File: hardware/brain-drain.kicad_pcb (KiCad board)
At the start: 4 copper layers, 180 x 110 mm, 310 parts, among them J10 SATA 22-pin, J11 SATA 22-pin, J12 SATA 22-pin, J13 SATA 22-pin, J21 KPJX-4S-S, J3 microSD, J4 RJ45 GbE magjack UDE RB1-125B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, J40 Fan GND/5V/TACH/PWM, J41 OLED GND/VCC/SCL/SDA, J5 USB-C rpiboot, J50 M.2 M-key, J6 nRPIBOOT, J7 UART0 GND/TX/RX, M1 CM5002016 (J1), M2 CM5002016 (J2), Q1 2N7002, Q20 AO4407A, Q31 P-FET -30V 6A DFN3x3, Q32 P-FET -30V 6A DFN3x3, Q33 P-FET -30V 6A DFN3x3, Q34 P-FET -30V 6A DFN3x3, Q41 P-FET -30V 6A DFN3x3, Q42 P-FET -30V 6A DFN3x3, Q43 P-FET -30V 6A DFN3x3, Q44 P-FET -30V 6A DFN3x3, Q51 2N7002, Q52 2N7002, Q53 2N7002, Q54 2N7002, Q61 2N7002, Q62 2N7002, Q63 2N7002, Q64 2N7002, SW1 DIP x8, SW3 door microswitch, U1 USB5744/2G, U10 ASM1153E, U11 ASM1153E, U12 ASM1153E, U13 ASM1153E, U2 USB5744/2G, U20 TPS56637RPAR, U21 TPS56637RPAR, U22 AP63203WU-7, U3 AP2112K-1.2, U50 TPS22965DSGR, U51 AP63203WU-7, Y1 25MHz CL=20pF, Y10 30MHz CL=16pF, Y11 30MHz CL=16pF, Y12 30MHz CL=16pF, Y13 30MHz CL=16pF, Y2 25MHz CL=20pF

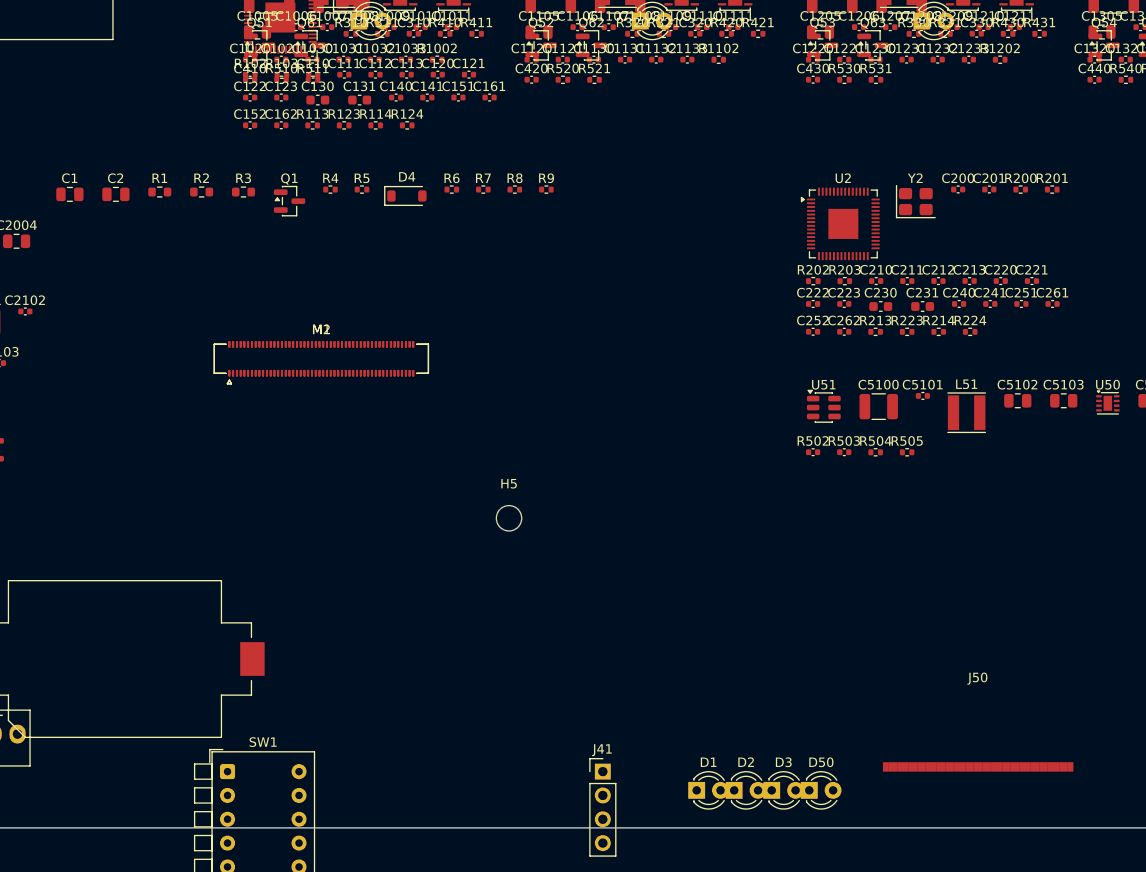
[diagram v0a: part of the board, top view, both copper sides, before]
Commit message: hardware: CM5 on the official 204-pad footprint, CM5IO M.2 footprint, reference-design fixes
From the Raspberry Pi CM5IO rev 2 KiCad files: single CM5 footprint with both
connectors and mounting holes; M.2 socket footprint; USB-C CC pins to the CM5;
fan PWM pull-up; microSD through a load switch on SD_PWR_ON; M.2 shield and
standoff pads to GND; PCIe polarity note. Board regenerated with the module
and M.2 at their real sizes; centre mounting hole dropped.

Co-Authored-By: Claude Fable 5.1 <noreply@anthropic.com>
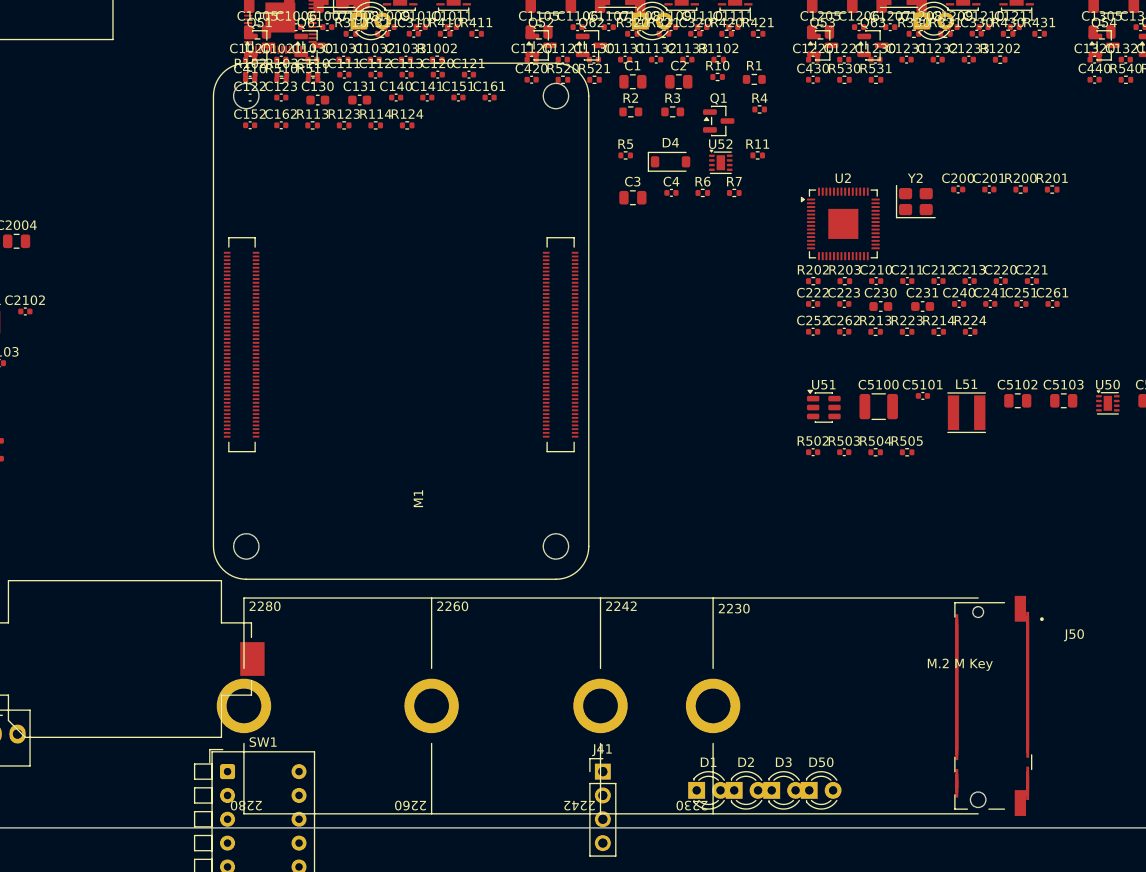
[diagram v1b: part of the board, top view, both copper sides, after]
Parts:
- added SW3: door microswitch, Button_Switch_THT:SW_PUSH_6mm, F.Cu at (196.0, 110.0)
- BT1: renamed from C1; value 22u 10V -> CR2032; footprint Capacitor_SMD:C_0805_2012Metric -> Battery:BatteryHolder_Keystone_1060_1x2032
- BZ1: renamed from SW1; value DIP x8 -> 5V magnetic; footprint Button_Switch_THT:SW_DIP_SPSTx08_Piano_10.8x21.88mm_W7.62mm_P2.54mm -> Buzzer_Beeper:Buzzer_12x9.5RM7.6
- C1: renamed from M1; value CM5002016 (J1) -> 22u 10V; footprint Connector_Hirose_DF40:Hirose_DF40C-100DS-0.4V_2x50_P0.4mm -> Capacitor_SMD:C_0805_2012Metric
- C1001: renamed from R1000; value 12.1k 1% -> 22p; footprint Resistor_SMD:R_0402_1005Metric -> Capacitor_SMD:C_0402_1005Metric
- C1002: renamed from L10; value 4.7u 1A -> 2.2u; footprint Inductor_SMD:L_Taiyo-Yuden_NR-40xx -> Capacitor_SMD:C_0603_1608Metric
- C1005: renamed from C1006; value 100n -> 10u 10V; footprint Capacitor_SMD:C_0402_1005Metric -> Capacitor_SMD:C_0805_2012Metric
- C101: renamed from R100; value 12.0k 1% -> 33p; footprint Resistor_SMD:R_0402_1005Metric -> Capacitor_SMD:C_0402_1005Metric
- C1021: renamed from C1030; value 10n -> 100n
- C1033: renamed from D10; value blue bay activity -> 10n; footprint LED_THT:LED_D3.0mm -> Capacitor_SMD:C_0402_1005Metric
- C1101: renamed from R1100; value 12.1k 1% -> 22p; footprint Resistor_SMD:R_0402_1005Metric -> Capacitor_SMD:C_0402_1005Metric
- C1102: renamed from L11; value 4.7u 1A -> 2.2u; footprint Inductor_SMD:L_Taiyo-Yuden_NR-40xx -> Capacitor_SMD:C_0603_1608Metric
- C1105: renamed from C1106; value 100n -> 10u 10V; footprint Capacitor_SMD:C_0402_1005Metric -> Capacitor_SMD:C_0805_2012Metric
- C1121: renamed from C1130; value 10n -> 100n
- C1133: renamed from D11; value blue bay activity -> 10n; footprint LED_THT:LED_D3.0mm -> Capacitor_SMD:C_0402_1005Metric
- C1201: renamed from R1200; value 12.1k 1% -> 22p; footprint Resistor_SMD:R_0402_1005Metric -> Capacitor_SMD:C_0402_1005Metric
- C1202: renamed from L12; value 4.7u 1A -> 2.2u; footprint Inductor_SMD:L_Taiyo-Yuden_NR-40xx -> Capacitor_SMD:C_0603_1608Metric
- C1205: renamed from C1206; value 100n -> 10u 10V; footprint Capacitor_SMD:C_0402_1005Metric -> Capacitor_SMD:C_0805_2012Metric
- C1221: renamed from C1230; value 10n -> 100n
- C123: renamed from C130; value 4.7u 10V -> 100n; footprint Capacitor_SMD:C_0603_1608Metric -> Capacitor_SMD:C_0402_1005Metric
- C1233: renamed from D12; value blue bay activity -> 10n; footprint LED_THT:LED_D3.0mm -> Capacitor_SMD:C_0402_1005Metric
- C1301: renamed from R1300; value 12.1k 1% -> 22p; footprint Resistor_SMD:R_0402_1005Metric -> Capacitor_SMD:C_0402_1005Metric
- C1302: renamed from L13; value 4.7u 1A -> 2.2u; footprint Inductor_SMD:L_Taiyo-Yuden_NR-40xx -> Capacitor_SMD:C_0603_1608Metric
- C1305: renamed from C1306; value 100n -> 10u 10V; footprint Capacitor_SMD:C_0402_1005Metric -> Capacitor_SMD:C_0805_2012Metric
- C131: renamed from C140; value 100n -> 4.7u 10V; footprint Capacitor_SMD:C_0402_1005Metric -> Capacitor_SMD:C_0603_1608Metric
- C1321: renamed from C1330; value 10n -> 100n
- C1333: renamed from D13; value blue bay activity -> 10n; footprint LED_THT:LED_D3.0mm -> Capacitor_SMD:C_0402_1005Metric
- C162: renamed from R113; value 10k -> 100n; footprint Resistor_SMD:R_0402_1005Metric -> Capacitor_SMD:C_0402_1005Metric
- C2: renamed from M2; value CM5002016 (J2) -> 22u 10V; footprint Connector_Hirose_DF40:Hirose_DF40C-100DS-0.4V_2x50_P0.4mm -> Capacitor_SMD:C_0805_2012Metric
- C20: renamed from D21; value 12V 0.5W -> 680u 25V low-ESR; footprint Diode_SMD:D_SOD-123 -> Capacitor_SMD:CP_Elec_10x10.5
- C2000: renamed from U20; value TPS56637RPAR -> 10u 25V; footprint brain-drain:Texas_RPA0010A_VQFN-HR-10_3x3mm -> Capacitor_SMD:C_1210_3225Metric
- C2002: renamed from C2001; value 10u 25V -> 100n 25V; footprint Capacitor_SMD:C_1210_3225Metric -> Capacitor_SMD:C_0402_1005Metric
- C2003: renamed from L20; value 2.2u 8A -> 22u 10V; footprint Inductor_SMD:L_Taiyo-Yuden_NR-60xx -> Capacitor_SMD:C_0805_2012Metric
- C201: renamed from R200; value 12.0k 1% -> 33p; footprint Resistor_SMD:R_0402_1005Metric -> Capacitor_SMD:C_0402_1005Metric
- C2100: renamed from U21; value TPS56637RPAR -> 10u 25V; footprint brain-drain:Texas_RPA0010A_VQFN-HR-10_3x3mm -> Capacitor_SMD:C_1210_3225Metric
- C2102: renamed from C2101; value 10u 25V -> 100n 25V; footprint Capacitor_SMD:C_1210_3225Metric -> Capacitor_SMD:C_0402_1005Metric
- C2103: renamed from L21; value 2.2u 8A -> 22u 10V; footprint Inductor_SMD:L_Taiyo-Yuden_NR-60xx -> Capacitor_SMD:C_0805_2012Metric
- C22: renamed from C21; value 680u 25V low-ESR -> 10u 25V; footprint Capacitor_SMD:CP_Elec_10x10.5 -> Capacitor_SMD:C_1210_3225Metric
- C2200: renamed from U22; value AP63203WU-7 -> 10u 25V; footprint Package_TO_SOT_SMD:TSOT-23-6 -> Capacitor_SMD:C_1210_3225Metric
- C2201: renamed from C2200; value 10u 25V -> 100n 10V; footprint Capacitor_SMD:C_1210_3225Metric -> Capacitor_SMD:C_0402_1005Metric
- C2202: renamed from L22; value 4.7u 3A -> 22u 10V; footprint Inductor_SMD:L_Taiyo-Yuden_NR-40xx -> Capacitor_SMD:C_0805_2012Metric
- C223: renamed from C230; value 4.7u 10V -> 100n; footprint Capacitor_SMD:C_0603_1608Metric -> Capacitor_SMD:C_0402_1005Metric
- C231: renamed from C240; value 100n -> 4.7u 10V; footprint Capacitor_SMD:C_0402_1005Metric -> Capacitor_SMD:C_0603_1608Metric
- C262: renamed from R213; value 10k -> 100n; footprint Resistor_SMD:R_0402_1005Metric -> Capacitor_SMD:C_0402_1005Metric
- C3: renamed from R6; value 470 -> 10u 10V; footprint Resistor_SMD:R_0402_1005Metric -> Capacitor_SMD:C_0805_2012Metric
- C30: renamed from U3; value AP2112K-1.2 -> 1u 10V; footprint Package_TO_SOT_SMD:SOT-23-5 -> Capacitor_SMD:C_0402_1005Metric
- C31: renamed from C30; value 1u 10V -> 10u 10V; footprint Capacitor_SMD:C_0402_1005Metric -> Capacitor_SMD:C_0805_2012Metric
- C310: renamed from R410; value 100k -> 100n; footprint Resistor_SMD:R_0402_1005Metric -> Capacitor_SMD:C_0402_1005Metric
- C320: renamed from R420; value 100k -> 100n; footprint Resistor_SMD:R_0402_1005Metric -> Capacitor_SMD:C_0402_1005Metric
- C330: renamed from R430; value 100k -> 100n; footprint Resistor_SMD:R_0402_1005Metric -> Capacitor_SMD:C_0402_1005Metric
- C340: renamed from R440; value 100k -> 100n; footprint Resistor_SMD:R_0402_1005Metric -> Capacitor_SMD:C_0402_1005Metric
- C4: renamed from R7; value 470 -> 1u 10V; footprint Resistor_SMD:R_0402_1005Metric -> Capacitor_SMD:C_0402_1005Metric
- C410: renamed from R510; value 10k -> 100n; footprint Resistor_SMD:R_0402_1005Metric -> Capacitor_SMD:C_0402_1005Metric
- C420: renamed from R520; value 10k -> 100n; footprint Resistor_SMD:R_0402_1005Metric -> Capacitor_SMD:C_0402_1005Metric
- C430: renamed from R530; value 10k -> 100n; footprint Resistor_SMD:R_0402_1005Metric -> Capacitor_SMD:C_0402_1005Metric
- C440: renamed from R540; value 10k -> 100n; footprint Resistor_SMD:R_0402_1005Metric -> Capacitor_SMD:C_0402_1005Metric
- C500: renamed from C501; value 22u 10V -> 10u 10V
- C501: renamed from C502; value 1n -> 22u 10V; footprint Capacitor_SMD:C_0402_1005Metric -> Capacitor_SMD:C_0805_2012Metric
- C502: renamed from R500; value 10k -> 1n; footprint Resistor_SMD:R_0402_1005Metric -> Capacitor_SMD:C_0402_1005Metric
- C5100: renamed from U51; value AP63203WU-7 -> 10u 25V; footprint Package_TO_SOT_SMD:TSOT-23-6 -> Capacitor_SMD:C_1210_3225Metric
- C5101: renamed from C5100; value 10u 25V -> 100n 10V; footprint Capacitor_SMD:C_1210_3225Metric -> Capacitor_SMD:C_0402_1005Metric
- C5102: renamed from L51; value 4.7u 3A -> 22u 10V; footprint Inductor_SMD:L_Taiyo-Yuden_NR-40xx -> Capacitor_SMD:C_0805_2012Metric
- D1: renamed from J40; value Fan GND/5V/TACH/PWM -> green PWR; footprint Connector:FanPinHeader_1x04_P2.54mm_Vertical -> LED_THT:LED_D3.0mm
- D10: renamed from R1002; value 470 -> blue bay activity; footprint Resistor_SMD:R_0402_1005Metric -> LED_THT:LED_D3.0mm
- D11: renamed from R1102; value 470 -> blue bay activity; footprint Resistor_SMD:R_0402_1005Metric -> LED_THT:LED_D3.0mm
- D12: renamed from R1202; value 470 -> blue bay activity; footprint Resistor_SMD:R_0402_1005Metric -> LED_THT:LED_D3.0mm
- D13: renamed from R1302; value 470 -> blue bay activity; footprint Resistor_SMD:R_0402_1005Metric -> LED_THT:LED_D3.0mm
- D2: renamed from R1; value 1k -> green ACT; footprint Resistor_SMD:R_0603_1608Metric -> LED_THT:LED_D3.0mm
- D20: renamed from F1; value 10A slow 0453010.MR -> SMBJ15A; footprint Fuse:Fuse_Littelfuse-NANO2-451_453 -> Diode_SMD:D_SMB
- D21: renamed from R20; value 100k -> 12V 0.5W; footprint Resistor_SMD:R_0603_1608Metric -> Diode_SMD:D_SOD-123
- D3: renamed from R2; value 1k -> red STATUS; footprint Resistor_SMD:R_0603_1608Metric -> LED_THT:LED_D3.0mm
- D4: renamed from R5; value 100k -> 1N4148W; footprint Resistor_SMD:R_0402_1005Metric -> Diode_SMD:D_SOD-123
- D50: renamed from SW3; value door microswitch -> blue M.2 activity; footprint Button_Switch_THT:SW_PUSH_6mm -> LED_THT:LED_D3.0mm
- F1: renamed from J21; value KPJX-4S-S -> 10A slow 0453010.MR; footprint brain-drain:Kycon_KPJX-4S-S -> Fuse:Fuse_Littelfuse-NANO2-451_453
- F10: renamed from F14; value 2A hold 1812 -> 3A hold 1812
- F11: renamed from F15; value 2A hold 1812 -> 3A hold 1812
- F12: renamed from F16; value 2A hold 1812 -> 3A hold 1812
- F13: renamed from F17; value 2A hold 1812 -> 3A hold 1812
- F14: renamed from U11; value ASM1153E -> 2A hold 1812; footprint Package_DFN_QFN:QFN-48-1EP_6x6mm_P0.4mm_EP4.6x4.6mm -> Fuse:Fuse_1812_4532Metric
- F15: renamed from U12; value ASM1153E -> 2A hold 1812; footprint Package_DFN_QFN:QFN-48-1EP_6x6mm_P0.4mm_EP4.6x4.6mm -> Fuse:Fuse_1812_4532Metric
- F16: renamed from U13; value ASM1153E -> 2A hold 1812; footprint Package_DFN_QFN:QFN-48-1EP_6x6mm_P0.4mm_EP4.6x4.6mm -> Fuse:Fuse_1812_4532Metric
- F17: renamed from Q31; value P-FET -30V 6A DFN3x3 -> 2A hold 1812; footprint Package_DFN_QFN:DFN-8-1EP_3x3mm_P0.65mm_EP1.5x2.25mm -> Fuse:Fuse_1812_4532Metric
- J10: renamed from Y10; value 30MHz CL=16pF -> SATA 22-pin; footprint Crystal:Crystal_SMD_3225-4Pin_3.2x2.5mm -> brain-drain:SATA_22pin_Receptacle_RA
- J11: renamed from Y11; value 30MHz CL=16pF -> SATA 22-pin; footprint Crystal:Crystal_SMD_3225-4Pin_3.2x2.5mm -> brain-drain:SATA_22pin_Receptacle_RA
- J12: renamed from Y12; value 30MHz CL=16pF -> SATA 22-pin; footprint Crystal:Crystal_SMD_3225-4Pin_3.2x2.5mm -> brain-drain:SATA_22pin_Receptacle_RA
- J13: renamed from Y13; value 30MHz CL=16pF -> SATA 22-pin; footprint Crystal:Crystal_SMD_3225-4Pin_3.2x2.5mm -> brain-drain:SATA_22pin_Receptacle_RA
- J21: renamed from H5; value M2.5 -> KPJX-4S-S; footprint MountingHole:MountingHole_2.7mm_M2.5 -> brain-drain:Kycon_KPJX-4S-S
- J3: renamed from J41; value OLED GND/VCC/SCL/SDA -> microSD; footprint Connector_PinHeader_2.54mm:PinHeader_1x04_P2.54mm_Vertical -> Connector_Card:microSD_HC_Hirose_DM3AT-SF-PEJM5
- J4: renamed from J5; value USB-C rpiboot -> RJ45 GbE magjack UDE RB1-125B8G1A; footprint Connector_USB:USB_C_Receptacle_GCT_USB4085 -> Connector_RJ:RJ45_UDE_RB1-125B8G1A
- J40: renamed from J6; value nRPIBOOT -> Fan GND/5V/TACH/PWM; footprint Connector_PinHeader_2.54mm:PinHeader_1x02_P2.54mm_Vertical -> Connector:FanPinHeader_1x04_P2.54mm_Vertical
- J41: renamed from D4; value 1N4148W -> OLED GND/VCC/SCL/SDA; footprint Diode_SMD:D_SOD-123 -> Connector_PinHeader_2.54mm:PinHeader_1x04_P2.54mm_Vertical
- J5: renamed from U1; value USB5744/2G -> USB-C rpiboot; footprint Package_DFN_QFN:QFN-56-1EP_7x7mm_P0.4mm_EP3.2x3.2mm -> Connector_USB:USB_C_Receptacle_GCT_USB4085
- J50: renamed from U50; value TPS22965DSGR -> M.2 M-key; footprint Package_SON:Texas_DSG0008A_WSON-8-1EP_2x2mm_P0.5mm_EP0.9x1.6mm -> brain-drain:M2_Socket3_MKey_CM5IO
- J6: renamed from C2; value 22u 10V -> nRPIBOOT; footprint Capacitor_SMD:C_0805_2012Metric -> Connector_PinHeader_2.54mm:PinHeader_1x02_P2.54mm_Vertical
- J7: renamed from BT1; value CR2032 -> UART0 GND/TX/RX; footprint Battery:BatteryHolder_Keystone_1060_1x2032 -> Connector_PinHeader_2.54mm:PinHeader_1x03_P2.54mm_Vertical
- L10: renamed from C1003; value 10u 10V -> 4.7u 1A; footprint Capacitor_SMD:C_0805_2012Metric -> Inductor_SMD:L_Taiyo-Yuden_NR-40xx
- L11: renamed from C1103; value 10u 10V -> 4.7u 1A; footprint Capacitor_SMD:C_0805_2012Metric -> Inductor_SMD:L_Taiyo-Yuden_NR-40xx
- L12: renamed from C1203; value 10u 10V -> 4.7u 1A; footprint Capacitor_SMD:C_0805_2012Metric -> Inductor_SMD:L_Taiyo-Yuden_NR-40xx
- L13: renamed from C1303; value 10u 10V -> 4.7u 1A; footprint Capacitor_SMD:C_0805_2012Metric -> Inductor_SMD:L_Taiyo-Yuden_NR-40xx
- L20: renamed from C2002; value 100n 25V -> 2.2u 8A; footprint Capacitor_SMD:C_0402_1005Metric -> Inductor_SMD:L_Taiyo-Yuden_NR-60xx
- L21: renamed from C2102; value 100n 25V -> 2.2u 8A; footprint Capacitor_SMD:C_0402_1005Metric -> Inductor_SMD:L_Taiyo-Yuden_NR-60xx
- L22: renamed from C2201; value 100n 10V -> 4.7u 3A; footprint Capacitor_SMD:C_0402_1005Metric -> Inductor_SMD:L_Taiyo-Yuden_NR-40xx
- L51: renamed from C5101; value 100n 10V -> 4.7u 3A; footprint Capacitor_SMD:C_0402_1005Metric -> Inductor_SMD:L_Taiyo-Yuden_NR-40xx
- M1: renamed from C31; value 10u 10V -> CM5002016; footprint Capacitor_SMD:C_0805_2012Metric -> brain-drain:Raspberry-Pi-5-Compute-Module
- Q1: renamed from BZ1; value 5V magnetic -> 2N7002; footprint Buzzer_Beeper:Buzzer_12x9.5RM7.6 -> Package_TO_SOT_SMD:SOT-23
- Q20: renamed from D20; value SMBJ15A -> AO4407A; footprint Diode_SMD:D_SMB -> Package_SO:SOIC-8_3.9x4.9mm_P1.27mm
- Q41: renamed from Q51; value 2N7002 -> P-FET -30V 6A DFN3x3; footprint Package_TO_SOT_SMD:SOT-23 -> Package_DFN_QFN:DFN-8-1EP_3x3mm_P0.65mm_EP1.5x2.25mm
- Q42: renamed from Q52; value 2N7002 -> P-FET -30V 6A DFN3x3; footprint Package_TO_SOT_SMD:SOT-23 -> Package_DFN_QFN:DFN-8-1EP_3x3mm_P0.65mm_EP1.5x2.25mm
- Q43: renamed from Q53; value 2N7002 -> P-FET -30V 6A DFN3x3; footprint Package_TO_SOT_SMD:SOT-23 -> Package_DFN_QFN:DFN-8-1EP_3x3mm_P0.65mm_EP1.5x2.25mm
- Q44: renamed from Q54; value 2N7002 -> P-FET -30V 6A DFN3x3; footprint Package_TO_SOT_SMD:SOT-23 -> Package_DFN_QFN:DFN-8-1EP_3x3mm_P0.65mm_EP1.5x2.25mm
- Q61: renamed from R310; value 100k -> 2N7002; footprint Resistor_SMD:R_0402_1005Metric -> Package_TO_SOT_SMD:SOT-23
- Q62: renamed from R320; value 100k -> 2N7002; footprint Resistor_SMD:R_0402_1005Metric -> Package_TO_SOT_SMD:SOT-23
- Q63: renamed from R330; value 100k -> 2N7002; footprint Resistor_SMD:R_0402_1005Metric -> Package_TO_SOT_SMD:SOT-23
- Q64: renamed from R340; value 100k -> 2N7002; footprint Resistor_SMD:R_0402_1005Metric -> Package_TO_SOT_SMD:SOT-23
- R1: renamed from D1; value green PWR -> 1k; footprint LED_THT:LED_D3.0mm -> Resistor_SMD:R_0603_1608Metric
- R10: renamed from J7; value UART0 GND/TX/RX -> 10k; footprint Connector_PinHeader_2.54mm:PinHeader_1x03_P2.54mm_Vertical -> Resistor_SMD:R_0402_1005Metric
- R100: renamed from R101; value 10k -> 12.0k 1%
- R1000: renamed from R1001; value 10k -> 12.1k 1%
- R1001: renamed from C1002; value 2.2u -> 10k; footprint Capacitor_SMD:C_0603_1608Metric -> Resistor_SMD:R_0402_1005Metric
- R1002: renamed from F10; value 3A hold 1812 -> 470; footprint Fuse:Fuse_1812_4532Metric -> Resistor_SMD:R_0402_1005Metric
- R102: renamed from R103; value 200k -> 10k
- R103: renamed from C110; value 100n -> 200k; footprint Capacitor_SMD:C_0402_1005Metric -> Resistor_SMD:R_0402_1005Metric
- R11: renamed from J4; value RJ45 GbE magjack UDE RB1-125B8G1A -> 10k; footprint Connector_RJ:RJ45_UDE_RB1-125B8G1A -> Resistor_SMD:R_0402_1005Metric
- R1100: renamed from R1101; value 10k -> 12.1k 1%
- R1101: renamed from C1102; value 2.2u -> 10k; footprint Capacitor_SMD:C_0603_1608Metric -> Resistor_SMD:R_0402_1005Metric
- R1102: renamed from F11; value 3A hold 1812 -> 470; footprint Fuse:Fuse_1812_4532Metric -> Resistor_SMD:R_0402_1005Metric
- R1200: renamed from R1201; value 10k -> 12.1k 1%
- R1201: renamed from C1202; value 2.2u -> 10k; footprint Capacitor_SMD:C_0603_1608Metric -> Resistor_SMD:R_0402_1005Metric
- R1202: renamed from F12; value 3A hold 1812 -> 470; footprint Fuse:Fuse_1812_4532Metric -> Resistor_SMD:R_0402_1005Metric
- R124: renamed from U2; value USB5744/2G -> 10k; footprint Package_DFN_QFN:QFN-56-1EP_7x7mm_P0.4mm_EP3.2x3.2mm -> Resistor_SMD:R_0402_1005Metric
- R1300: renamed from R1301; value 10k -> 12.1k 1%
- R1301: renamed from C1302; value 2.2u -> 10k; footprint Capacitor_SMD:C_0603_1608Metric -> Resistor_SMD:R_0402_1005Metric
- R1302: renamed from F13; value 3A hold 1812 -> 470; footprint Fuse:Fuse_1812_4532Metric -> Resistor_SMD:R_0402_1005Metric
- R2: renamed from D2; value green ACT -> 1k; footprint LED_THT:LED_D3.0mm -> Resistor_SMD:R_0603_1608Metric
- R20: renamed from Q20; value AO4407A -> 100k; footprint Package_SO:SOIC-8_3.9x4.9mm_P1.27mm -> Resistor_SMD:R_0603_1608Metric
- R200: renamed from R201; value 10k -> 12.0k 1%
- R2000: renamed from C2005; value 22u 10V -> 73.2k; footprint Capacitor_SMD:C_0805_2012Metric -> Resistor_SMD:R_0402_1005Metric
- R2001: renamed from R2000; value 73.2k -> 10k
- R2002: renamed from R2001; value 10k -> 100k
- R2003: renamed from R2002; value 100k -> 10k
- R202: renamed from R203; value 200k -> 10k
- R203: renamed from C210; value 100n -> 200k; footprint Capacitor_SMD:C_0402_1005Metric -> Resistor_SMD:R_0402_1005Metric
- R2100: renamed from C2105; value 22u 10V -> 73.2k; footprint Capacitor_SMD:C_0805_2012Metric -> Resistor_SMD:R_0402_1005Metric
- R2101: renamed from R2100; value 73.2k -> 10k
- R2102: renamed from R2101; value 10k -> 100k
- R2103: renamed from R2102; value 100k -> 10k
- R224: renamed from U10; value ASM1153E -> 10k; footprint Package_DFN_QFN:QFN-48-1EP_6x6mm_P0.4mm_EP4.6x4.6mm -> Resistor_SMD:R_0402_1005Metric
- R3: renamed from D3; value red STATUS -> 1k; footprint LED_THT:LED_D3.0mm -> Resistor_SMD:R_0603_1608Metric
- R310: renamed from R311; value 10k -> 100k
- R311: renamed from C310; value 100n -> 10k; footprint Capacitor_SMD:C_0402_1005Metric -> Resistor_SMD:R_0402_1005Metric
- R320: renamed from R321; value 10k -> 100k
- R321: renamed from C320; value 100n -> 10k; footprint Capacitor_SMD:C_0402_1005Metric -> Resistor_SMD:R_0402_1005Metric
- R330: renamed from R331; value 10k -> 100k
- R331: renamed from C330; value 100n -> 10k; footprint Capacitor_SMD:C_0402_1005Metric -> Resistor_SMD:R_0402_1005Metric
- R340: renamed from R341; value 10k -> 100k
- R341: renamed from C340; value 100n -> 10k; footprint Capacitor_SMD:C_0402_1005Metric -> Resistor_SMD:R_0402_1005Metric
- R4: renamed from Q1; value 2N7002 -> 1k; footprint Package_TO_SOT_SMD:SOT-23 -> Resistor_SMD:R_0402_1005Metric
- R410: renamed from R411; value 10k -> 100k
- R411: renamed from C410; value 100n -> 10k; footprint Capacitor_SMD:C_0402_1005Metric -> Resistor_SMD:R_0402_1005Metric
- R420: renamed from R421; value 10k -> 100k
- R421: renamed from C420; value 100n -> 10k; footprint Capacitor_SMD:C_0402_1005Metric -> Resistor_SMD:R_0402_1005Metric
- R430: renamed from R431; value 10k -> 100k
- R431: renamed from C430; value 100n -> 10k; footprint Capacitor_SMD:C_0402_1005Metric -> Resistor_SMD:R_0402_1005Metric
- R440: renamed from R441; value 10k -> 100k
- R441: renamed from C440; value 100n -> 10k; footprint Capacitor_SMD:C_0402_1005Metric -> Resistor_SMD:R_0402_1005Metric
- R5: renamed from R4; value 1k -> 100k
- R501: renamed from R502; value 0R (cap DNP alt) -> 10k; footprint Capacitor_SMD:C_0402_1005Metric -> Resistor_SMD:R_0402_1005Metric
- R503: renamed from R504; value 10k -> 0R (cap DNP alt); footprint Resistor_SMD:R_0402_1005Metric -> Capacitor_SMD:C_0402_1005Metric
- R504: renamed from R505; value 470 -> 10k
- R505: renamed from D50; value blue M.2 activity -> 470; footprint LED_THT:LED_D3.0mm -> Resistor_SMD:R_0402_1005Metric
- R510: renamed from R511; value 1k -> 10k
- R511: renamed from Q32; value P-FET -30V 6A DFN3x3 -> 1k; footprint Package_DFN_QFN:DFN-8-1EP_3x3mm_P0.65mm_EP1.5x2.25mm -> Resistor_SMD:R_0402_1005Metric
- R520: renamed from R521; value 1k -> 10k
- R521: renamed from Q33; value P-FET -30V 6A DFN3x3 -> 1k; footprint Package_DFN_QFN:DFN-8-1EP_3x3mm_P0.65mm_EP1.5x2.25mm -> Resistor_SMD:R_0402_1005Metric
- R530: renamed from R531; value 1k -> 10k
- R531: renamed from Q34; value P-FET -30V 6A DFN3x3 -> 1k; footprint Package_DFN_QFN:DFN-8-1EP_3x3mm_P0.65mm_EP1.5x2.25mm -> Resistor_SMD:R_0402_1005Metric
- R540: renamed from R541; value 1k -> 10k
- R541: renamed from J50; value M.2 M-key -> 1k; footprint brain-drain:M2_Socket3_MKey_4.2mm -> Resistor_SMD:R_0402_1005Metric
- R6: renamed from R8; value 5.1k -> 470
- R7: renamed from R9; value 5.1k -> 470
- SW1: renamed from R3; value 1k -> DIP x8; footprint Resistor_SMD:R_0603_1608Metric -> Button_Switch_THT:SW_DIP_SPSTx08_Piano_10.8x21.88mm_W7.62mm_P2.54mm
- U1: renamed from Y1; value 25MHz CL=20pF -> USB5744/2G; footprint Crystal:Crystal_SMD_3225-4Pin_3.2x2.5mm -> Package_DFN_QFN:QFN-56-1EP_7x7mm_P0.4mm_EP3.2x3.2mm
- U10: renamed from J10; value SATA 22-pin -> ASM1153E; footprint brain-drain:SATA_22pin_Receptacle_RA -> Package_DFN_QFN:QFN-48-1EP_6x6mm_P0.4mm_EP4.6x4.6mm
- U11: renamed from J11; value SATA 22-pin -> ASM1153E; footprint brain-drain:SATA_22pin_Receptacle_RA -> Package_DFN_QFN:QFN-48-1EP_6x6mm_P0.4mm_EP4.6x4.6mm
- U12: renamed from J12; value SATA 22-pin -> ASM1153E; footprint brain-drain:SATA_22pin_Receptacle_RA -> Package_DFN_QFN:QFN-48-1EP_6x6mm_P0.4mm_EP4.6x4.6mm
- U13: renamed from J13; value SATA 22-pin -> ASM1153E; footprint brain-drain:SATA_22pin_Receptacle_RA -> Package_DFN_QFN:QFN-48-1EP_6x6mm_P0.4mm_EP4.6x4.6mm
- U2: renamed from Y2; value 25MHz CL=20pF -> USB5744/2G; footprint Crystal:Crystal_SMD_3225-4Pin_3.2x2.5mm -> Package_DFN_QFN:QFN-56-1EP_7x7mm_P0.4mm_EP3.2x3.2mm
- U20: renamed from C22; value 10u 25V -> TPS56637RPAR; footprint Capacitor_SMD:C_1210_3225Metric -> brain-drain:Texas_RPA0010A_VQFN-HR-10_3x3mm
- U21: renamed from R2003; value 10k -> TPS56637RPAR; footprint Resistor_SMD:R_0402_1005Metric -> brain-drain:Texas_RPA0010A_VQFN-HR-10_3x3mm
- U22: renamed from R2103; value 10k -> AP63203WU-7; footprint Resistor_SMD:R_0402_1005Metric -> Package_TO_SOT_SMD:TSOT-23-6
- U3: renamed from C5103; value 22u 10V -> AP2112K-1.2; footprint Capacitor_SMD:C_0805_2012Metric -> Package_TO_SOT_SMD:SOT-23-5
- U50: renamed from C500; value 10u 10V -> TPS22965DSGR; footprint Capacitor_SMD:C_0805_2012Metric -> Package_SON:Texas_DSG0008A_WSON-8-1EP_2x2mm_P0.5mm_EP0.9x1.6mm
- U51: renamed from C2203; value 22u 10V -> AP63203WU-7; footprint Capacitor_SMD:C_0805_2012Metric -> Package_TO_SOT_SMD:TSOT-23-6
- U52: renamed from J3; value microSD -> TPS22965DSGR; footprint Connector_Card:microSD_HC_Hirose_DM3AT-SF-PEJM5 -> Package_SON:Texas_DSG0008A_WSON-8-1EP_2x2mm_P0.5mm_EP0.9x1.6mm
- Y1: renamed from C100; value 33p -> 25MHz CL=20pF; footprint Capacitor_SMD:C_0402_1005Metric -> Crystal:Crystal_SMD_3225-4Pin_3.2x2.5mm
- Y10: renamed from C1000; value 22p -> 30MHz CL=16pF; footprint Capacitor_SMD:C_0402_1005Metric -> Crystal:Crystal_SMD_3225-4Pin_3.2x2.5mm
- Y11: renamed from C1100; value 22p -> 30MHz CL=16pF; footprint Capacitor_SMD:C_0402_1005Metric -> Crystal:Crystal_SMD_3225-4Pin_3.2x2.5mm
- Y12: renamed from C1200; value 22p -> 30MHz CL=16pF; footprint Capacitor_SMD:C_0402_1005Metric -> Crystal:Crystal_SMD_3225-4Pin_3.2x2.5mm
- Y13: renamed from C1300; value 22p -> 30MHz CL=16pF; footprint Capacitor_SMD:C_0402_1005Metric -> Crystal:Crystal_SMD_3225-4Pin_3.2x2.5mm
- Y2: renamed from C200; value 33p -> 25MHz CL=20pF; footprint Capacitor_SMD:C_0402_1005Metric -> Crystal:Crystal_SMD_3225-4Pin_3.2x2.5mm
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- renumbered C101 to C100, C1001 to C1000, C1004 to C1003, C1005 to C1004, C1007 to C1006, C1008 to C1007, C1009 to C1008, C1010 to C1009, C1011 to C1010, C1020 to C1011, C1021 to C1020, C1031 to C1030, C1032 to C1031, C1033 to C1032, C111 to C110, C1101 to C1100, C1104 to C1103, C1105 to C1104, C1107 to C1106, C1108 to C1107, C1109 to C1108, C1110 to C1109, C112 to C111, C1111 to C1110, C1120 to C1111, C113 to C112, C1121 to C1120, C120 to C113, C1131 to C1130, C1132 to C1131, C1133 to C1132, C121 to C120, C1201 to C1200, C1204 to C1203, C1205 to C1204, C1207 to C1206, C1208 to C1207, C1209 to C1208, C1210 to C1209, C122 to C121, C1211 to C1210, C1220 to C1211, C123 to C122, C1221 to C1220, C1231 to C1230, C1232 to C1231, C1233 to C1232, C131 to C130, C1301 to C1300, C1304 to C1303, C1305 to C1304, C1307 to C1306, C1308 to C1307, C1309 to C1308, C1310 to C1309, C1311 to C1310, C1320 to C1311, C1321 to C1320, C1331 to C1330, C1332 to C1331, C1333 to C1332, C141 to C140, C151 to C141, C161 to C151, C162 to C152, C152 to C161, C201 to C200, C2000 to C2001, C2003 to C2004, C2004 to C2005, C20 to C21, C211 to C210, C2100 to C2101, C2103 to C2104, C2104 to C2105, C212 to C211, C213 to C212, C220 to C213, C221 to C220, C2202 to C2203, C222 to C221, C223 to C222, C231 to C230, C241 to C240, C251 to C241, C261 to C251, C262 to C252, C252 to C261, C5102 to C5103, Q41 to Q31, Q42 to Q32, Q43 to Q33, Q44 to Q34, Q61 to Q51, Q62 to Q52, Q63 to Q53, Q64 to Q54, R102 to R101, R123 to R113, R124 to R114, R114 to R123, R202 to R201, R223 to R213, R224 to R214, R214 to R223, R501 to R500, R503 to R502
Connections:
- BT1 pad 1: 5V_SYS -> VBAT
- BZ1 pad 1: DIP1 -> 5V_SYS
- BZ1 pad 2: DIP2 -> BZ1_N
- C1 pad 1: GND -> 5V_SYS
- C100 pad 1: U1_XTALO -> U1_XTALI
- C1000 pad 1: U10_XO -> U10_XI
- C1001 pad 1: U10_REXT -> U10_XO
- C1002 pad 1: U10_LXI -> U10_RST
- C1002 pad 2: U10_VDD_CORE -> GND
- C1003 pad 1: 5V_SYS -> U10_VDD_CORE
- C1004 pad 1: U10_VCCO -> 5V_SYS
- C1005 pad 1: U10_VDD_CORE -> U10_VCCO
- C1007 pad 1: U10_VCCO -> U10_VDD_CORE
- C101 pad 1: U1_RBIAS -> U1_XTALO
- C1011 pad 1: U10_UTXP -> U10_VCCO
- C1011 pad 2: BAY1_USB3_TX_P -> GND
- C1020 pad 1: U10_UTXN -> U10_UTXP
- C1020 pad 2: BAY1_USB3_TX_N -> BAY1_USB3_TX_P
- C1021 pad 1: U10_STXP -> U10_UTXN
- C1021 pad 2: BAY1_SATA_A_P -> BAY1_USB3_TX_N
- C1030 pad 1: U10_STXN -> U10_STXP
- C1030 pad 2: BAY1_SATA_A_N -> BAY1_SATA_A_P
- C1031 pad 1: BAY1_SATA_B_P -> U10_STXN
- C1031 pad 2: U10_SRXP -> BAY1_SATA_A_N
- C1032 pad 1: BAY1_SATA_B_N -> BAY1_SATA_B_P
- C1032 pad 2: U10_SRXN -> U10_SRXP
- C1033 pad 1: U10_LED -> BAY1_SATA_B_N
- C1033 pad 2: BAY1_LED_A -> U10_SRXN
- C1100 pad 1: U11_XO -> U11_XI
- C1101 pad 1: U11_REXT -> U11_XO
- C1102 pad 1: U11_LXI -> U11_RST
- C1102 pad 2: U11_VDD_CORE -> GND
- C1103 pad 1: 5V_SYS -> U11_VDD_CORE
- C1104 pad 1: U11_VCCO -> 5V_SYS
- C1105 pad 1: U11_VDD_CORE -> U11_VCCO
- C1107 pad 1: U11_VCCO -> U11_VDD_CORE
- C1111 pad 1: U11_UTXP -> U11_VCCO
- C1111 pad 2: BAY2_USB3_TX_P -> GND
- C1120 pad 1: U11_UTXN -> U11_UTXP
- C1120 pad 2: BAY2_USB3_TX_N -> BAY2_USB3_TX_P
- C1121 pad 1: U11_STXP -> U11_UTXN
- C1121 pad 2: BAY2_SATA_A_P -> BAY2_USB3_TX_N
- C113 pad 1: +1V2 -> +3V3
- C1130 pad 1: U11_STXN -> U11_STXP
- C1130 pad 2: BAY2_SATA_A_N -> BAY2_SATA_A_P
- C1131 pad 1: BAY2_SATA_B_P -> U11_STXN
- C1131 pad 2: U11_SRXP -> BAY2_SATA_A_N
- C1132 pad 1: BAY2_SATA_B_N -> BAY2_SATA_B_P
- C1132 pad 2: U11_SRXN -> U11_SRXP
- C1133 pad 1: U11_LED -> BAY2_SATA_B_N
- C1133 pad 2: BAY2_LED_A -> U11_SRXN
- C1200 pad 1: U12_XO -> U12_XI
- C1201 pad 1: U12_REXT -> U12_XO
- C1202 pad 1: U12_LXI -> U12_RST
- C1202 pad 2: U12_VDD_CORE -> GND
- C1203 pad 1: 5V_SYS -> U12_VDD_CORE
- C1204 pad 1: U12_VCCO -> 5V_SYS
- C1205 pad 1: U12_VDD_CORE -> U12_VCCO
- C1207 pad 1: U12_VCCO -> U12_VDD_CORE
- C1211 pad 1: U12_UTXP -> U12_VCCO
- C1211 pad 2: BAY3_USB3_TX_P -> GND
- C1220 pad 1: U12_UTXN -> U12_UTXP
- C1220 pad 2: BAY3_USB3_TX_N -> BAY3_USB3_TX_P
- C1221 pad 1: U12_STXP -> U12_UTXN
- C1221 pad 2: BAY3_SATA_A_P -> BAY3_USB3_TX_N
- C123 pad 1: +3V3 -> +1V2
- C1230 pad 1: U12_STXN -> U12_STXP
- C1230 pad 2: BAY3_SATA_A_N -> BAY3_SATA_A_P
- C1231 pad 1: BAY3_SATA_B_P -> U12_STXN
- C1231 pad 2: U12_SRXP -> BAY3_SATA_A_N
- C1232 pad 1: BAY3_SATA_B_N -> BAY3_SATA_B_P
- C1232 pad 2: U12_SRXN -> U12_SRXP
- C1233 pad 1: U12_LED -> BAY3_SATA_B_N
- C1233 pad 2: BAY3_LED_A -> U12_SRXN
- C130 pad 1: +1V2 -> +3V3
- C1300 pad 1: U13_XO -> U13_XI
- C1301 pad 1: U13_REXT -> U13_XO
- C1302 pad 1: U13_LXI -> U13_RST
- C1302 pad 2: U13_VDD_CORE -> GND
- C1303 pad 1: 5V_SYS -> U13_VDD_CORE
- C1304 pad 1: U13_VCCO -> 5V_SYS
- C1305 pad 1: U13_VDD_CORE -> U13_VCCO
- C1307 pad 1: U13_VCCO -> U13_VDD_CORE
- C131 pad 1: U1_UP_TXDP -> +1V2
- C131 pad 2: USB3_0_RX_P -> GND
- C1311 pad 1: U13_UTXP -> U13_VCCO
- C1311 pad 2: BAY4_USB3_TX_P -> GND
- C1320 pad 1: U13_UTXN -> U13_UTXP
- C1320 pad 2: BAY4_USB3_TX_N -> BAY4_USB3_TX_P
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
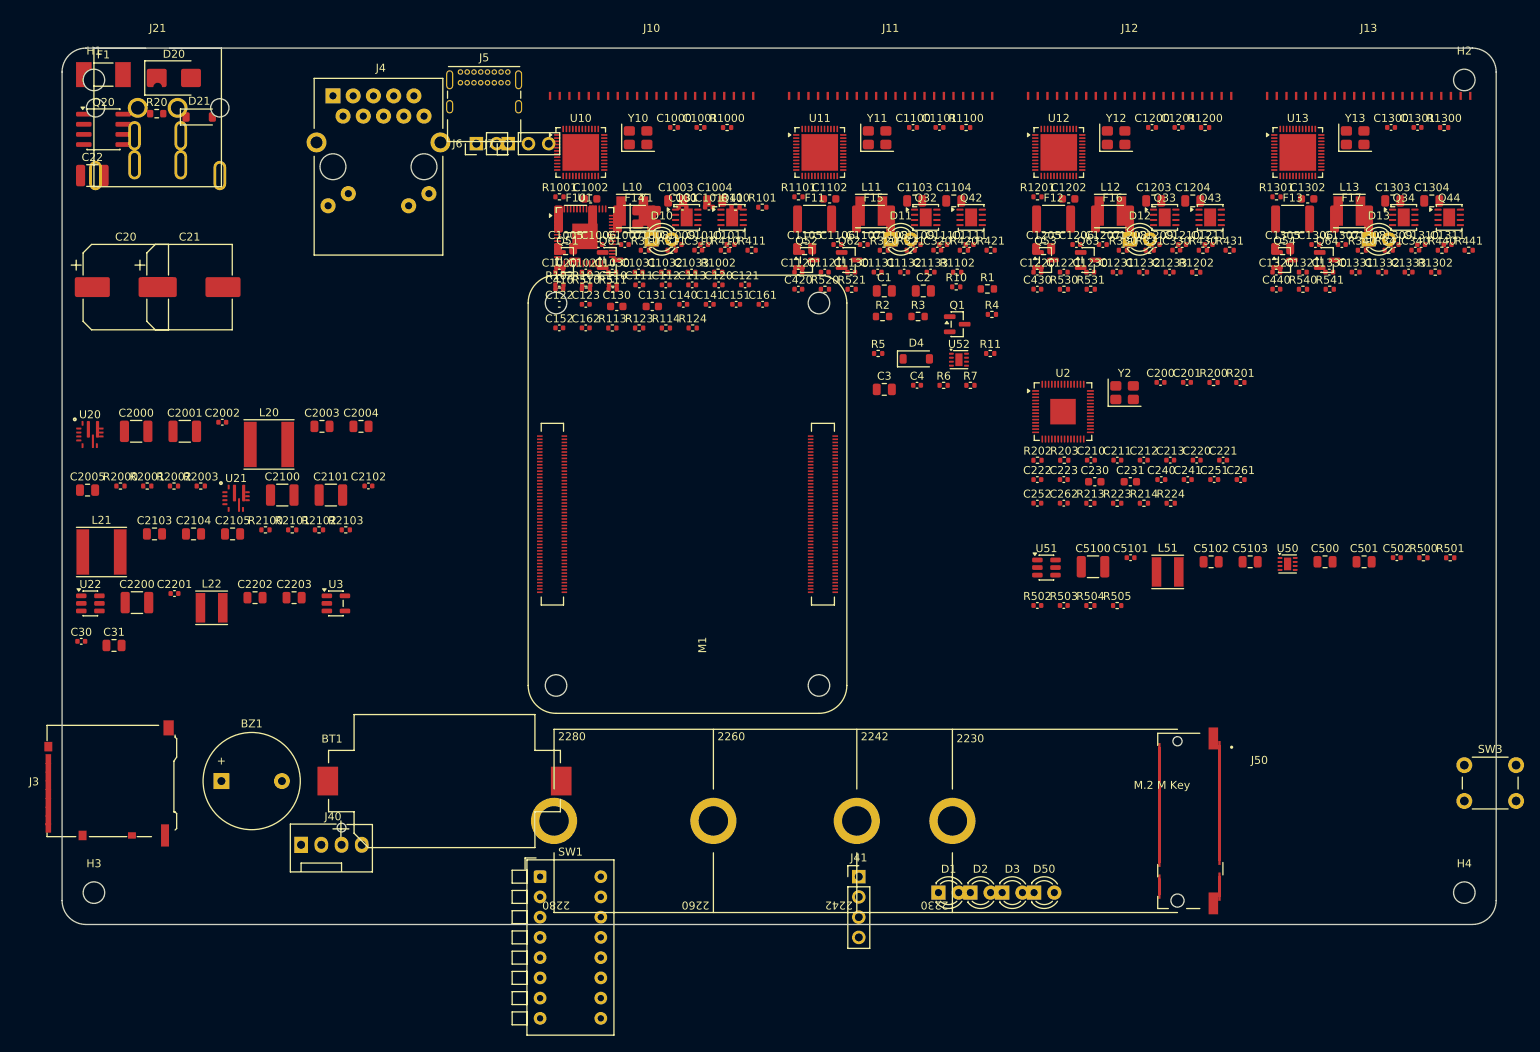
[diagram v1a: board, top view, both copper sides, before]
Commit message: hardware: board placement pass (M.2 inserts from the right wall, UI front-left, bridge regions resized)
Co-Authored-By: Claude Fable 5.1 <noreply@anthropic.com>
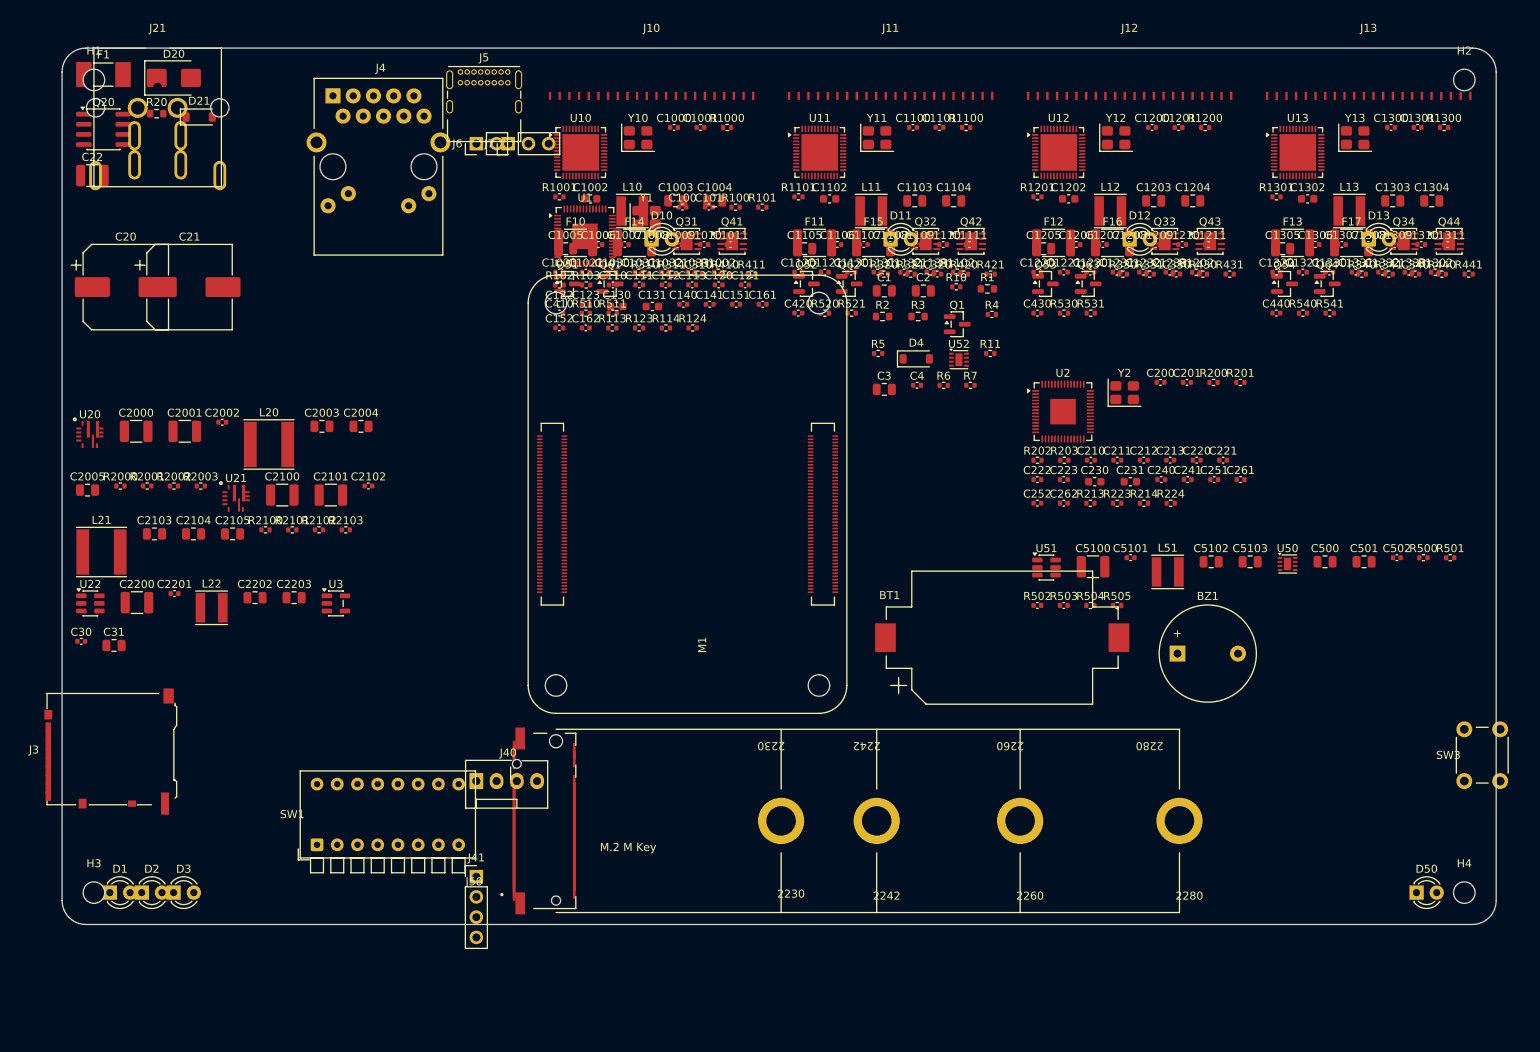
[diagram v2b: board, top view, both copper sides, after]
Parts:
- moved BZ1 121.1 mm to (160.0, 96.0)
- moved D1 104.0 mm to (26.0, 126.0)
- moved D2 104.0 mm to (30.0, 126.0)
- moved D3 104.0 mm to (34.0, 126.0)
- moved J50 78.0 mm to (82.0, 117.0), turned to 90 degrees
- moved BT1 72.3 mm to (138.0, 94.0)
- moved D50 48.0 mm to (190.0, 126.0)
- moved J41 48.0 mm to (72.0, 124.0)
- moved SW1 28.3 mm to (52.0, 120.0), turned to 90 degrees
- moved J40 23.4 mm to (72.0, 112.0)
- moved J3 4.00 mm to (26.0, 108.0)
- moved C310 3.00 mm to (99.8, 48.4)
- moved C320 3.00 mm to (129.8, 48.4)
- moved C330 3.00 mm to (159.8, 48.4)
- moved C340 3.00 mm to (189.8, 48.4)
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
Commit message: hardware: front-strip placement nudge
Co-Authored-By: Claude Fable 5.1 <noreply@anthropic.com>
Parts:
- moved J40 6.00 mm to (66.0, 112.0)
- moved J41 6.00 mm to (66.0, 124.0)
- moved SW1 4.00 mm to (48.0, 120.0)
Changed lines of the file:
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@@
 		(version 20241229)
 		(generator "pcbnew")
-		(at 72 112 0)
+		(at 66 112 0)
 		(generator_version "9.0")
 		(layer "F.Cu")
@@
 		(version 20241229)
 		(generator "kicad-footprint-generator")
-		(at 52 120 90)
+		(at 48 120 90)
 		(layer "F.Cu")
 		(descr "8x-dip-switch SPST , Piano, row spacing 7.62 mm (300 mils), body size 10.8x21.88mm")
@@
 		(version 20241229)
 		(generator "kicad-footprint-generator")
-		(at 72 124 0)
+		(at 66 124 0)
 		(layer "F.Cu")
 		(descr "Through hole straight pin header, 1x04, 2.54mm pitch, single row")
